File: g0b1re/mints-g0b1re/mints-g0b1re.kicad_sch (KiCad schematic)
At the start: 27 parts, among them J1 Conn_01x08, J2 Conn_01x04, J3 Conn_01x02, J4 Conn_01x04, J5 Conn_01x04, SW1 SW_Coded_SH-7050, U1 STM32G0B1RETx, U2 TCAN3414DDFR, U5 AP63203WU

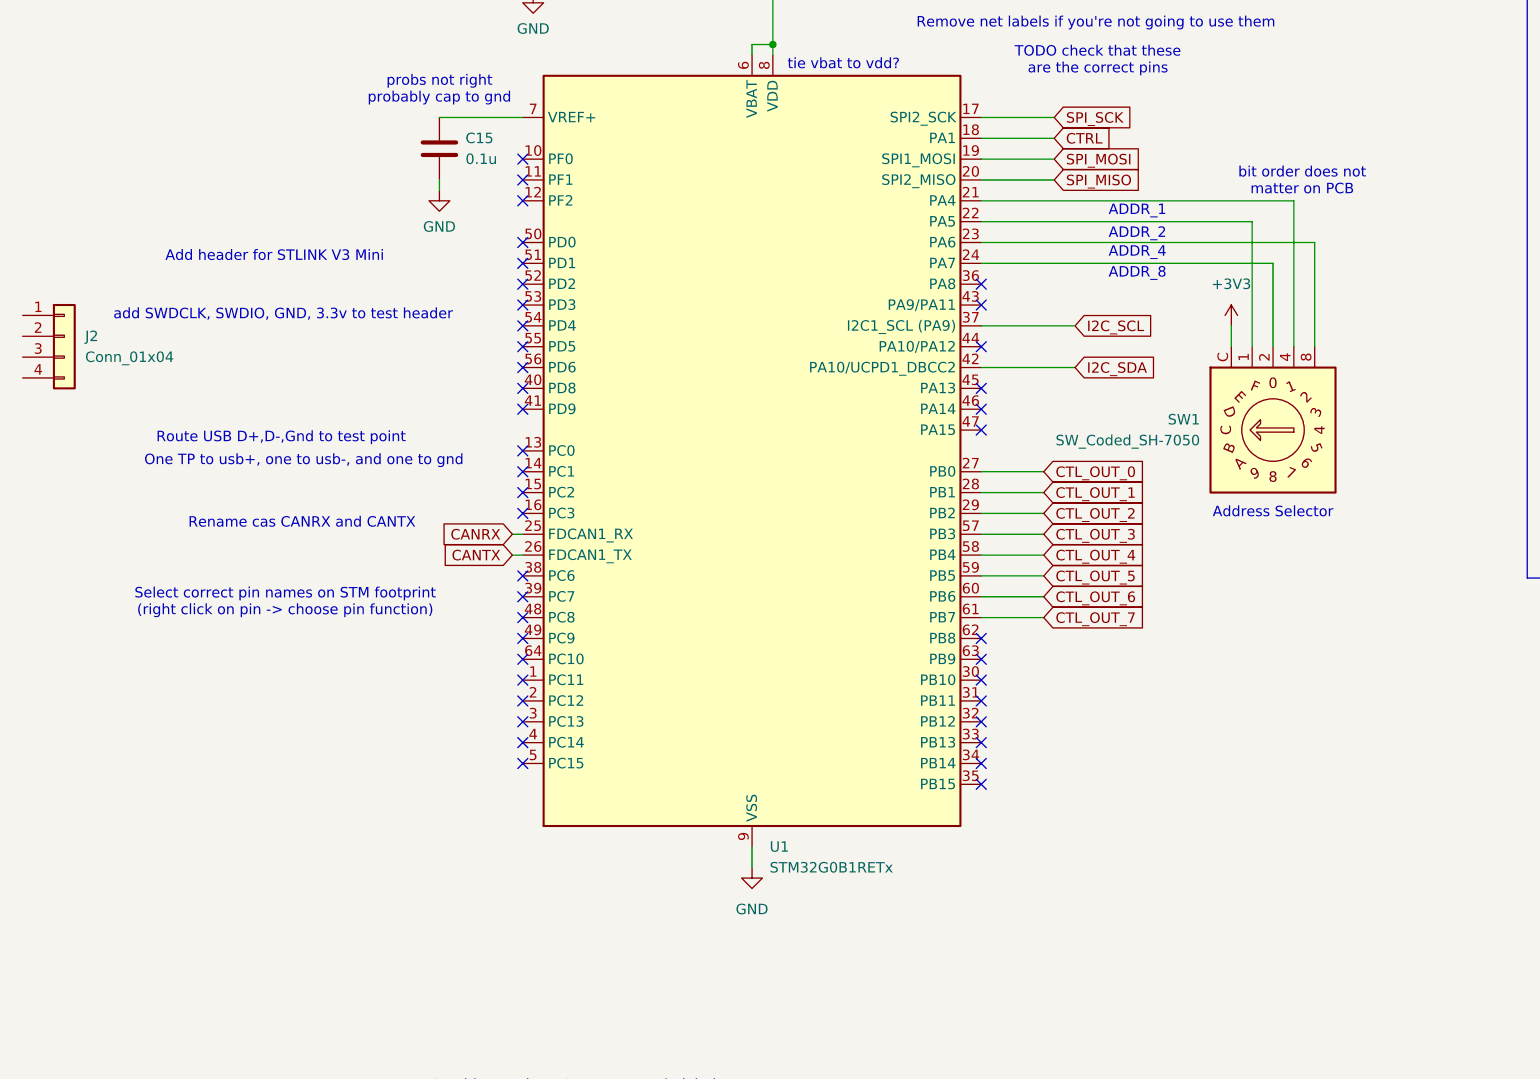
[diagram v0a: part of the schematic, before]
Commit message: Fix SPI, add status LED, move addr setter
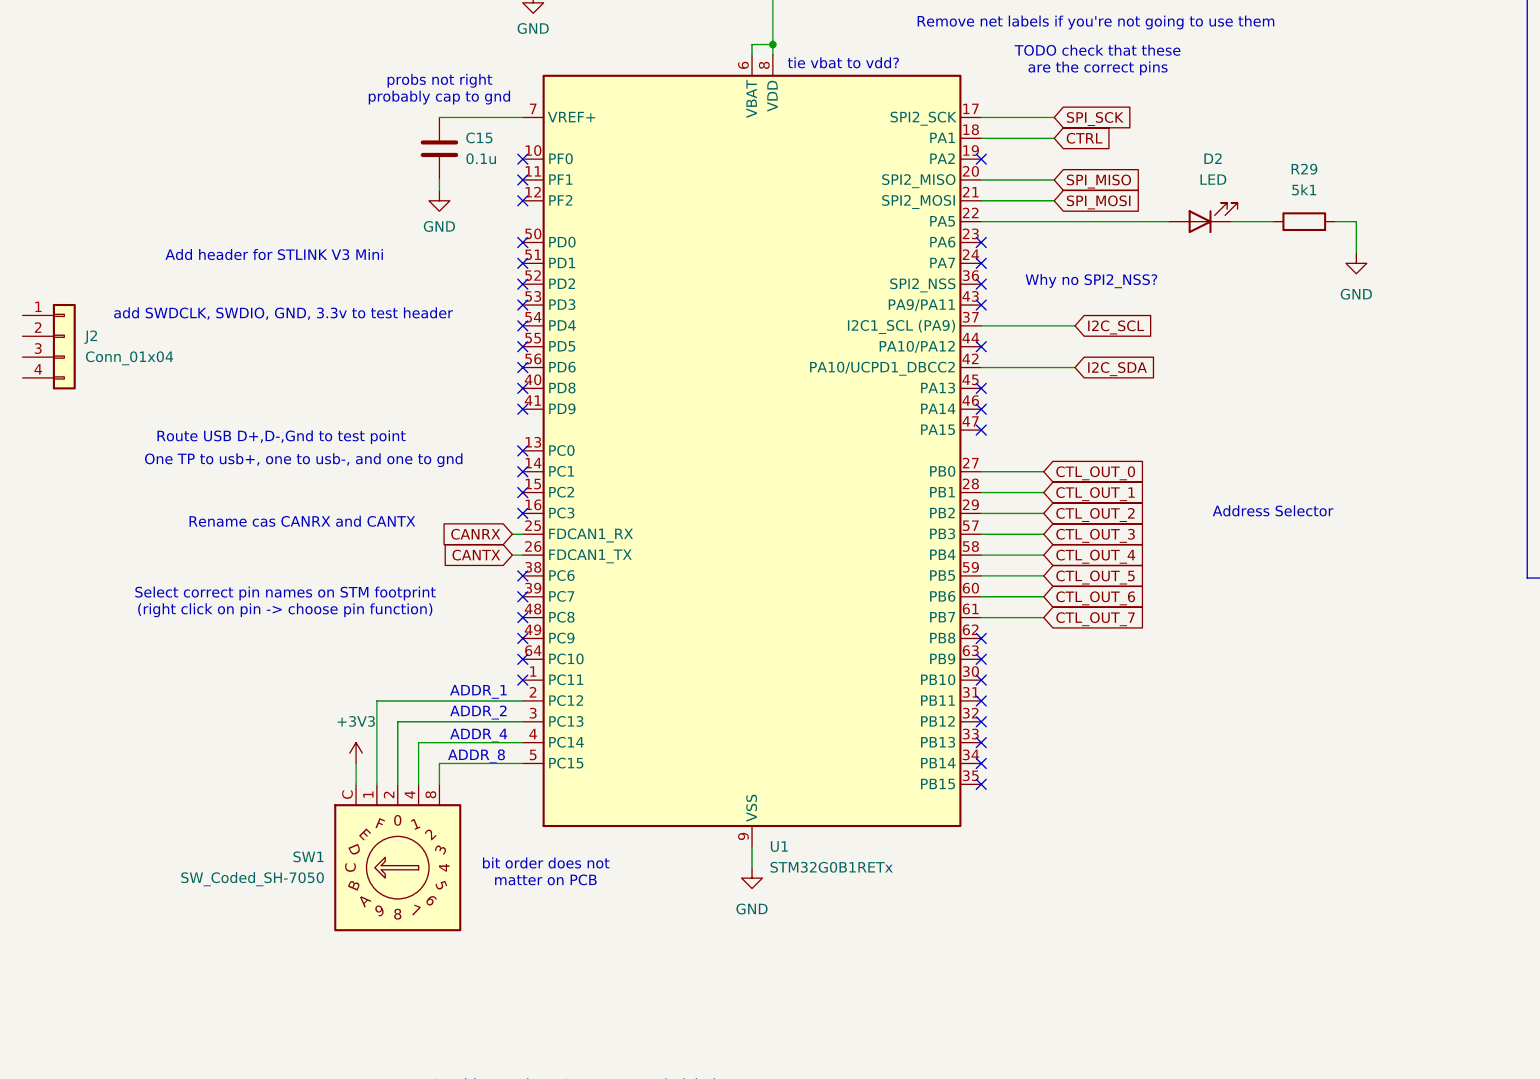
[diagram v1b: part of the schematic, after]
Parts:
- added D2: LED, symbol Device:LED
- added R29: 5k1, symbol Device:R
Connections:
- net GND: now also R29.2
- net SPI_MOSI: now also U1.21 (PA4); no longer U1.19 (PA2)
- net at U1.2 (PC12): now also SW1.1
- net at SW1.4: now also U1.4 (PC14); no longer U1.21 (PA4)
- net at U1.22 (PA5): now also D2.2 (A); no longer SW1.1
- net at U1.23 (PA6): no longer SW1.8
- net at U1.24 (PA7): no longer SW1.2
- net at U1.3 (PC13): now also SW1.2
- net at U1.5 (PC15): now also SW1.8
- new net: D2.1 (K), R29.1
- no-connect marks 40 -> 39
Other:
- note added: "Why no SPI2_NSS?"
- moved on the sheet: SW1

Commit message: Finished Schematic
Added STLINK header. Added flash header. Changed ADC. Fixed ESD caps.
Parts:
- added J6: FTSH-107-01-X-DV-K, FTSH-107-01-X-DV-K:SAMTEC_FTSH-107-01-X-DV-K, symbol FTSH-107-01-X-DV-K:FTSH-107-01-X-DV-K
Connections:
- net GND: now also U2.8 (STB)
- no-connect marks 39 -> 40
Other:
- moved on the sheet: J2

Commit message: Finished Schematic (missed save)
Same updates from previous commit.
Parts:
- removed J2: Conn_01x04, symbol Connector_Generic:Conn_01x04
- added J7: Conn_01x04, symbol Connector_Generic:Conn_01x04
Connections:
- net +3V3: now also J6.03, J7.1 (Pin_1)
- net CANRX: now also U1.26 (PC5); no longer U1.25 (PC4)
- net CANTX: now also U1.25 (PC4); no longer U1.26 (PC5)
- net GND: now also J6.05, J6.07, J7.4 (Pin_4)
- net NRST: now reaches U1.12 (PF2)
- net NRST: now also J6.12
- net SWDIO: now reaches U1.45 (PA13)
- net SWDIO: now also J6.04, J7.3 (Pin_3)
- net SWCLK: now reaches U1.46 (PA14)
- net SWCLK: now also J6.06, J7.2 (Pin_2)
- net VCP_RX: now reaches U1.52 (PD2)
- net VCP_RX: now also J6.13
- net VCP_TX: now reaches U1.53 (PD3)
- net VCP_TX: now also J6.14
- net EXTI: now reaches U1.54 (PD4)
- no-connect marks 40 -> 39
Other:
- note added: "10v"
- note added: "STLINK Header"
- moved on the sheet: C11, C12, C13, C14, C15, C5, C6, C7, C8, C9, D2, D3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
